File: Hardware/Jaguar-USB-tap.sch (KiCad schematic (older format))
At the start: 27 parts, among them J1 DB15, P1 CONN_01X03, P2 USB_B, P3 CONN_01X05, U1 NCP1117ST33T3G, U2 STM32F070F6, U3 TXB0106, U4 TXB0106, Y1 8MHz

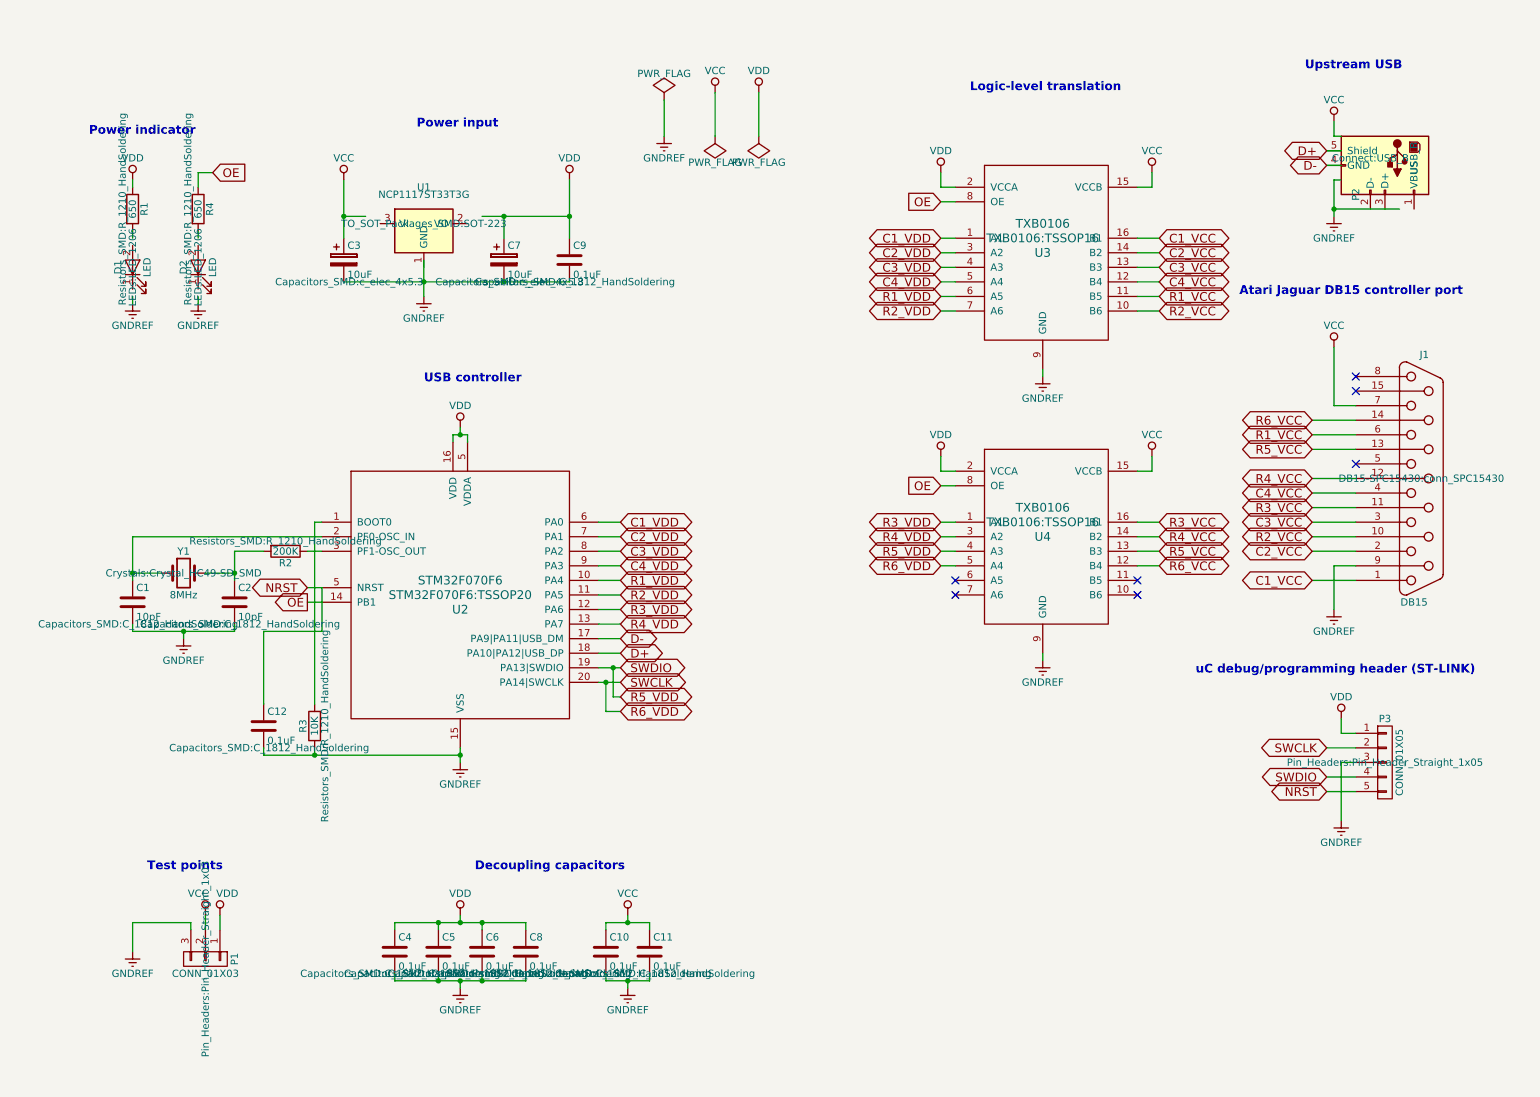
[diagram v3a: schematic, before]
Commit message: Rework schematic to fx hardware bugs and add features.
1) Add jumpers for OE to allow manual disabling of logic-level translator ICs.
2) Add RESET button.
3) Upgrade to larger STM32F07 series IC so ST-LINK SWD lines don't have to pull double-duty as general-purpose GPIO. Allows for continued debugging during operation.
4) Fix missing pin assignments in previous board which prevented proper powerng of uC.
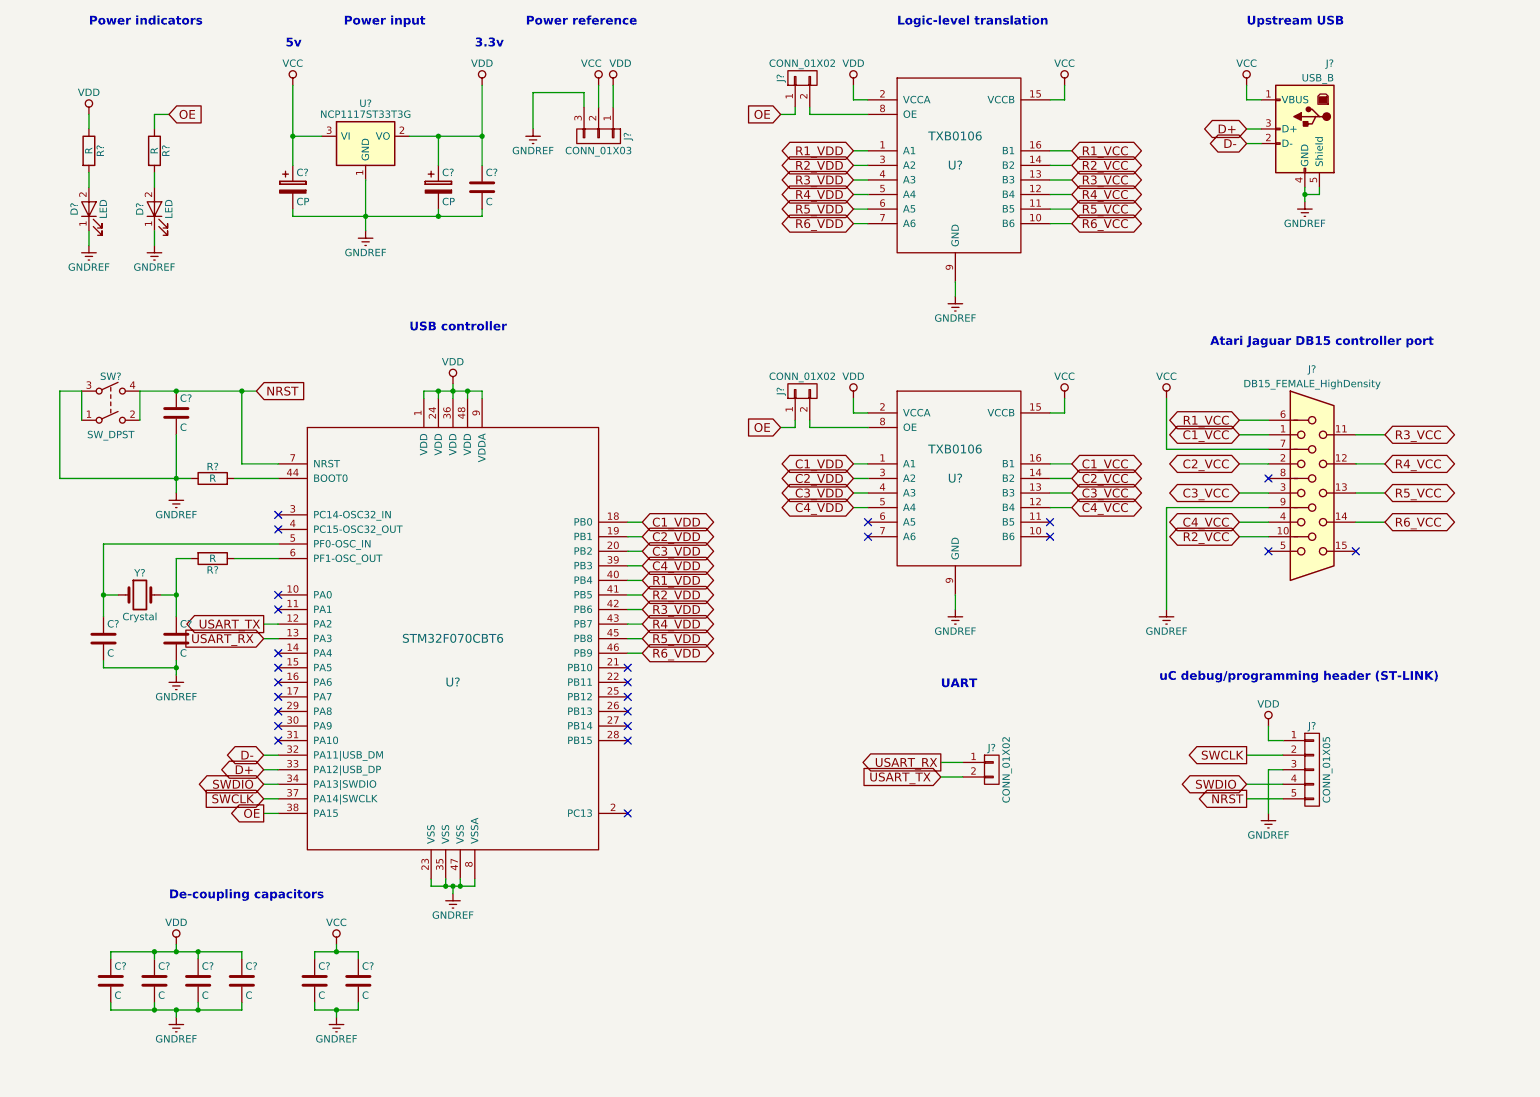
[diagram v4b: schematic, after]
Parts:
- removed C1, C2: 10pF, Capacitors_SMD:C_1812_HandSoldering, symbol C
- removed C10, C11, C12, C4, C5, C6, C8, C9: 0.1uF, Capacitors_SMD:C_1812_HandSoldering, symbol C
- removed C3, C7: 10uF, Capacitors_SMD:c_elec_4x5.3, symbol CP
- removed D1, D2: LED, LEDs:LED_1206, symbol LED
- removed J1: DB15, DB15-SPC15430:conn_SPC15430, symbol DB15
- removed P1: CONN_01X03, Pin_Headers:Pin_Header_Straight_1x03, symbol CONN_01X03
- removed P2: USB_B, Connect:USB_B, symbol USB_B
- removed P3: CONN_01X05, Pin_Headers:Pin_Header_Straight_1x05, symbol CONN_01X05
- removed R1, R4: 650, Resistors_SMD:R_1210_HandSoldering, symbol R
- removed R2: 200K, Resistors_SMD:R_1210_HandSoldering, symbol R
- removed R3: 10K, Resistors_SMD:R_1210_HandSoldering, symbol R
- removed U1: NCP1117ST33T3G, TO_SOT_Packages_SMD:SOT-223, symbol NCP1117ST33T3G
- removed U2: STM32F070F6, STM32F070F6:TSSOP20, symbol STM32F070F6
- removed U3, U4: TXB0106, TXB0106:TSSOP16, symbol TXB0106
- removed Y1: 8MHz, Crystals:Crystal_HC49-SD_SMD, symbol Crystal
- added C? (x2): CP, symbol CP
- added C? (x10): C, symbol C
- added D? (x2): LED, symbol LED
- added J?: USB_B, symbol USB_B
- added J?: DB15_FEMALE_HighDensity, symbol DB15_FEMALE_HighDensity
- added J?: CONN_01X05, symbol CONN_01X05
- added J?: CONN_01X03, symbol CONN_01X03
- added J? (x3): CONN_01X02, symbol CONN_01X02
- added R? (x4): R, symbol R
- added SW?: SW_DPST, symbol SW_DPST
- added U?: STM32F070CBT6, symbol STM32F070CBT6
- added U? (x2): TXB0106, symbol TXB0106
- added U?: NCP1117ST33T3G, TO_SOT_Packages_SMD:SOT-223, symbol NCP1117ST33T3G
- added Y?: Crystal, symbol Crystal
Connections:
- net labels added: USART_RX, USART_TX
- wire segments 144 -> 159
- no-connect marks 7 -> 25
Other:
- note added: "3.3v"
- note added: "5v"
- note added: "De-coupling capacitors"
- note added: "Power indicators"
- note added: "Power reference"
- note added: "UART"
- note removed: "Decoupling capacitors"
- note removed: "Power indicator"
- note removed: "Test points"

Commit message: Start PCB layout of revised board.
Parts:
- removed SW?: SW_DPST, symbol SW_DPST
- added SW1: SW_DPST_x2, Buttons_Switches_THT:SW_PUSH_6mm, symbol SW_DPST_x2
- C1, C5: renamed from C?; value C -> 20pF; footprint (none) -> Capacitors_SMD:C_1812_HandSoldering
- C10, C12, C2, C3, C4, C6, C7, C9: renamed from C?; value C -> 0.1uF; footprint (none) -> Capacitors_SMD:C_1812_HandSoldering
- C11, C8: renamed from C?; value CP -> 10uF; footprint (none) -> Capacitors_SMD:CP_Elec_4x5.8
- D1, D2: renamed from D?; footprint (none) -> LEDs:LED_1206
- J1: renamed from J?; footprint (none) -> Pin_Headers:Pin_Header_Straight_1x03_Pitch2.54mm
- J2, J3, J4: renamed from J?; footprint (none) -> Pin_Headers:Pin_Header_Straight_1x02_Pitch2.54mm
- J5: renamed from J?; footprint (none) -> Connectors:USB_B
- J6: renamed from J?; footprint (none) -> DB15-SPC15430:conn_SPC15430
- J7: renamed from J?; footprint (none) -> Pin_Headers:Pin_Header_Straight_1x05_Pitch2.54mm
- R1, R2: renamed from R?; value R -> 650; footprint (none) -> Resistors_SMD:R_1210_HandSoldering
- R3: renamed from R?; value R -> 10K; footprint (none) -> Resistors_SMD:R_1210_HandSoldering
- R4: renamed from R?; value R -> 200K; footprint (none) -> Resistors_SMD:R_1210_HandSoldering
- U2: renamed from U?; footprint (none) -> Housings_QFP:LQFP-48_7x7mm_Pitch0.5mm
- U3, U4: renamed from U?; footprint (none) -> TXB0106:TSSOP16
- Y1: renamed from Y?; value Crystal -> 8MHz; footprint (none) -> Crystals:Crystal_SMD_HC49-SD_HandSoldering
- gave numbers to parts that had none: 1
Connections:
- net GNDREF: now also SW1.1 (A)
- net NRST: now also SW1.2 (B)

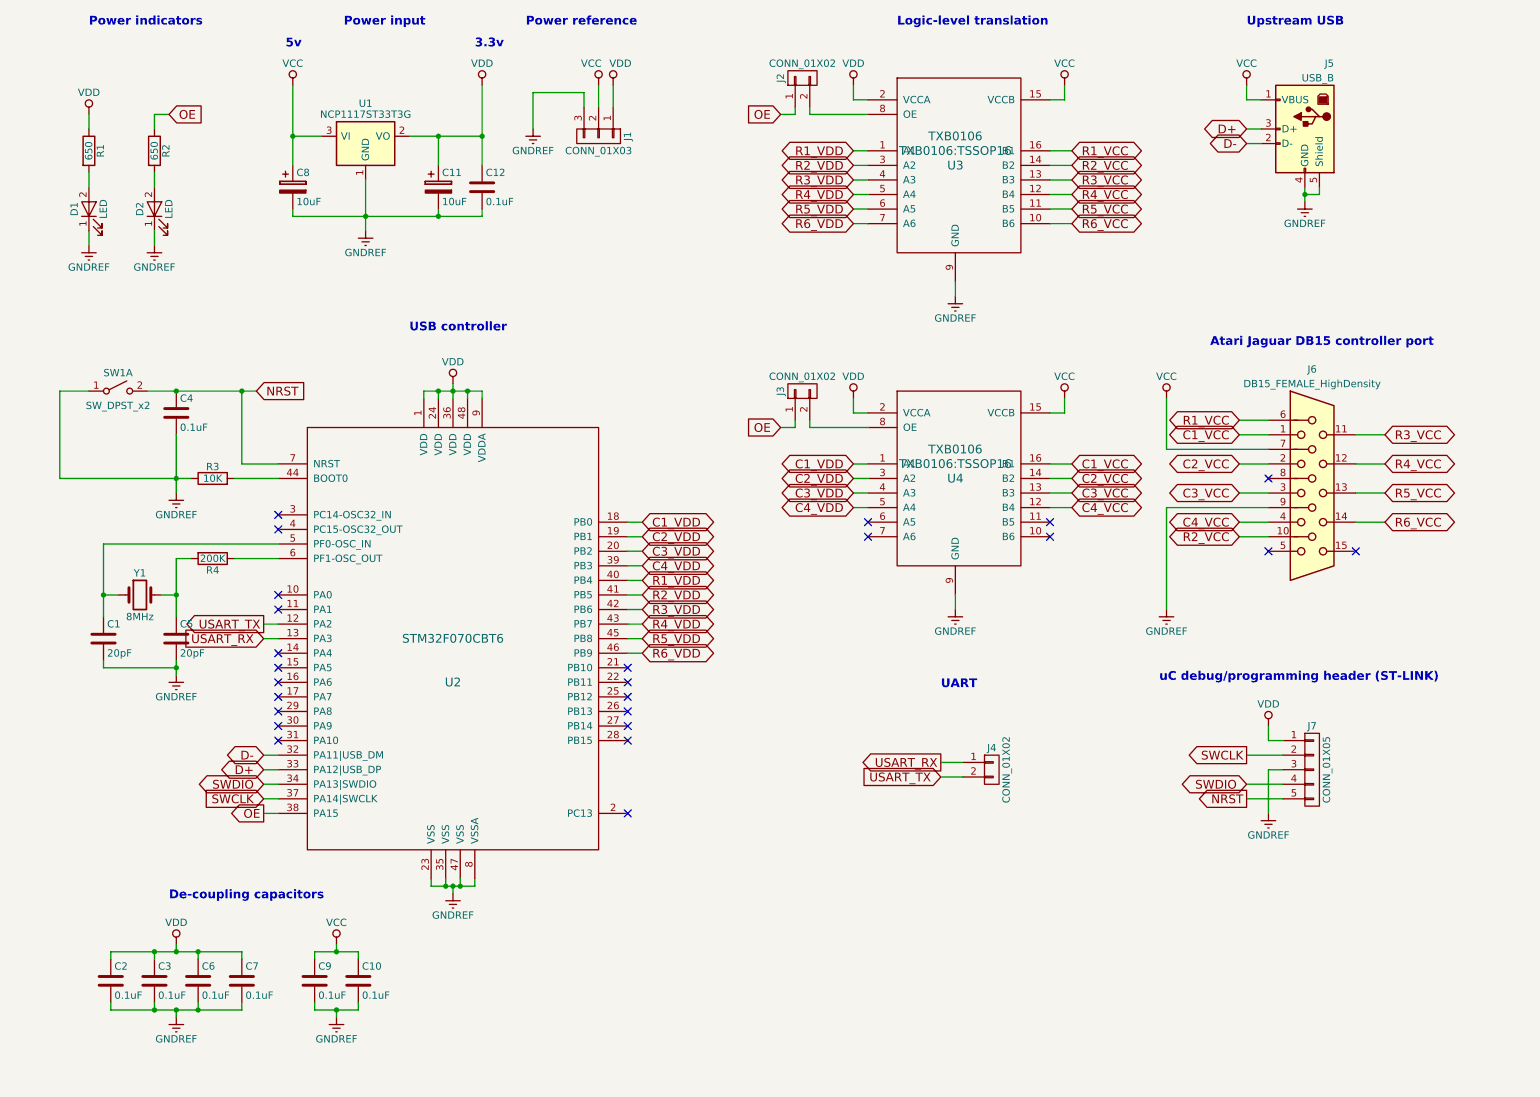
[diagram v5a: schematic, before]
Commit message: Remove logic-level translation ICs and drive teh controller at 3.3v directly from the uC.
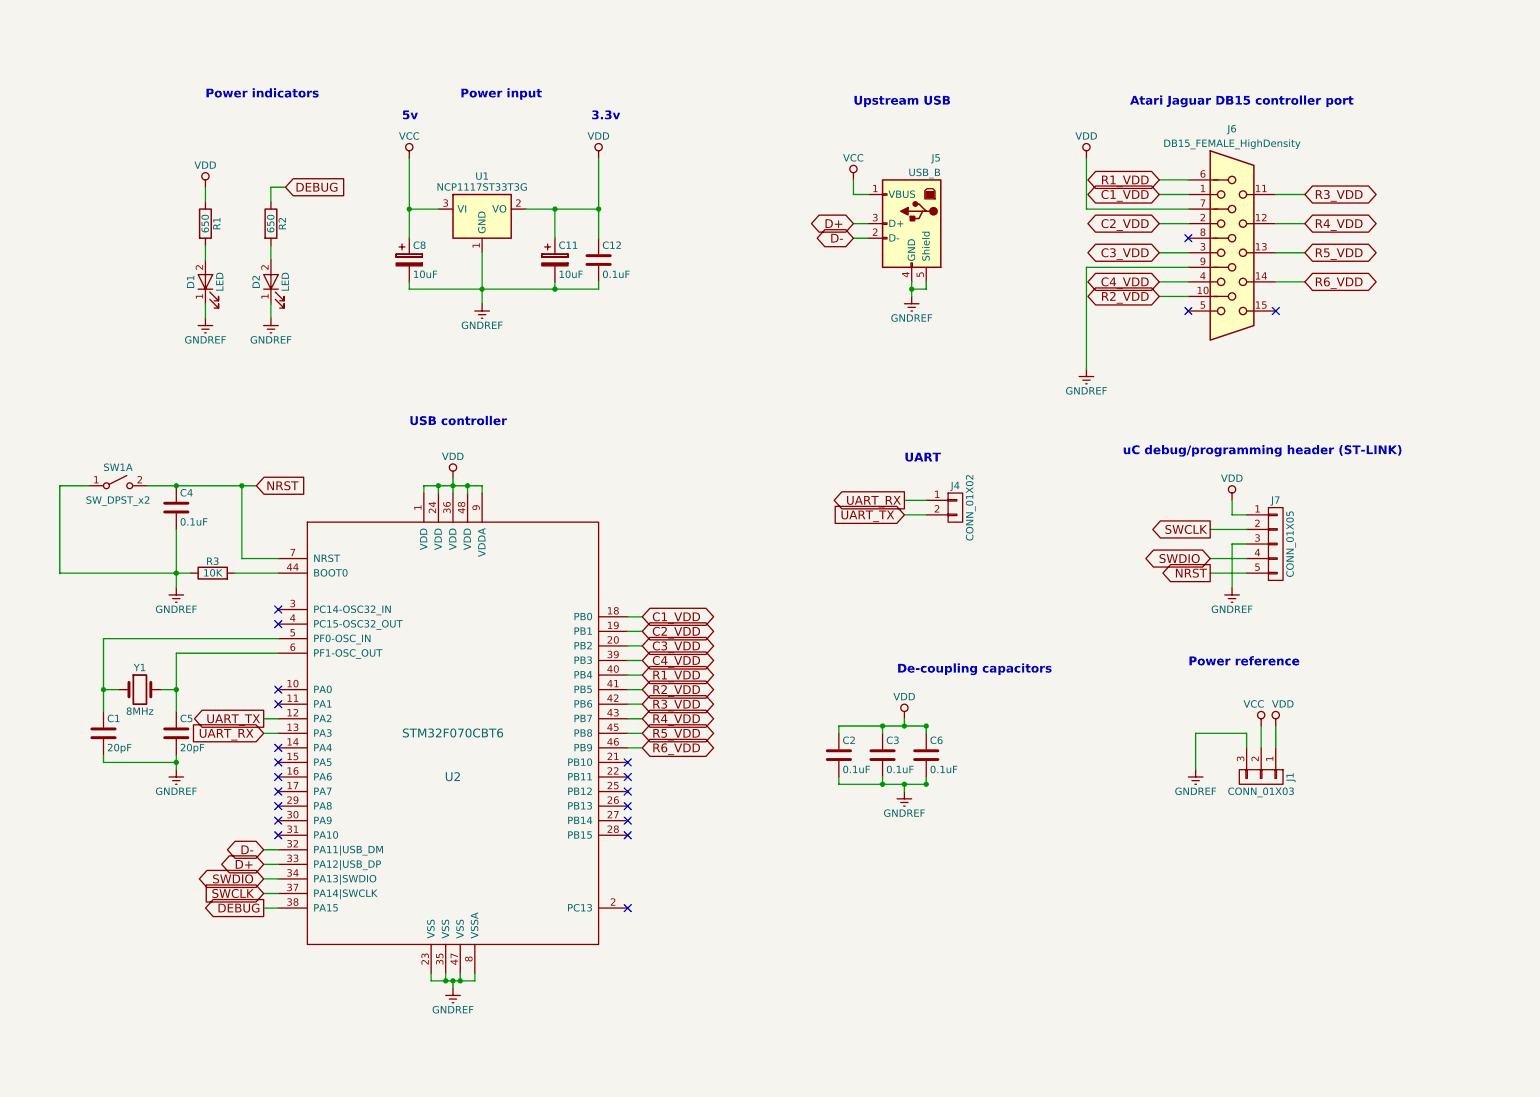
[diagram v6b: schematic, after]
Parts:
- removed C10, C7, C9: 0.1uF, Capacitors_SMD:C_1812_HandSoldering, symbol C
- removed J2, J3: CONN_01X02, Pin_Headers:Pin_Header_Straight_1x02_Pitch2.54mm, symbol CONN_01X02
- removed R4: 200K, Resistors_SMD:R_1210_HandSoldering, symbol R
- removed U3, U4: TXB0106, TXB0106:TSSOP16, symbol TXB0106
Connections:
- net C1_VCC is gone; now on net C1_VDD: J6.1
- net C2_VCC is gone; now on net C2_VDD: J6.2
- net C3_VCC is gone; now on net C3_VDD: J6.3
- net C4_VCC is gone; now on net C4_VDD: J6.4
- net R1_VCC is gone; now on net R1_VDD: J6.6
- net R2_VCC is gone; now on net R2_VDD: J6.10
- net R3_VCC is gone; now on net R3_VDD: J6.11
- net R4_VCC is gone; now on net R4_VDD: J6.12
- net R5_VCC is gone; now on net R5_VDD: J6.13
- net R6_VCC is gone; now on net R6_VDD: J6.14
- net VCC: no longer J6.7
- net VDD: now also J6.7
- net at U2.6 (PF1-OSC_OUT): now also C5.1, Y1.2
- net OE renamed DEBUG
- net USART_RX renamed UART_RX
- net USART_TX renamed UART_TX
- no-connect marks 25 -> 21
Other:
- note removed: "Logic-level translation"
- moved on the sheet: C1, C11, C12, C2, C3, C4, C5, C6, C8, D1, D2, J1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
